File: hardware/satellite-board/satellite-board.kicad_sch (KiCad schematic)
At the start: 18 parts, among them J1 MTJ-88ARX1-FSM-LG, J2 B2B-PH-K-S, U1 LORA1262-915TCXO, U2 XC6220B331MR, U3 ESP32-C6-DEVKITC-1-N8, U4 MAX3485, U5 L70RE-M37

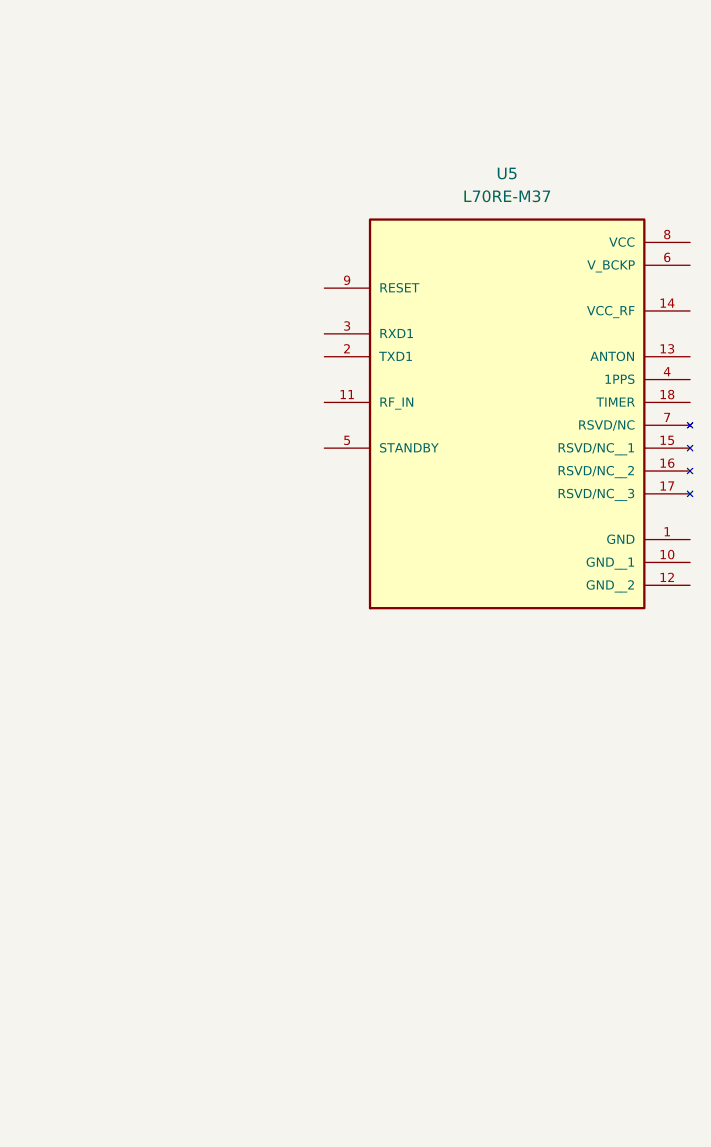
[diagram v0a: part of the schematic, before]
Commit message: New GPS module
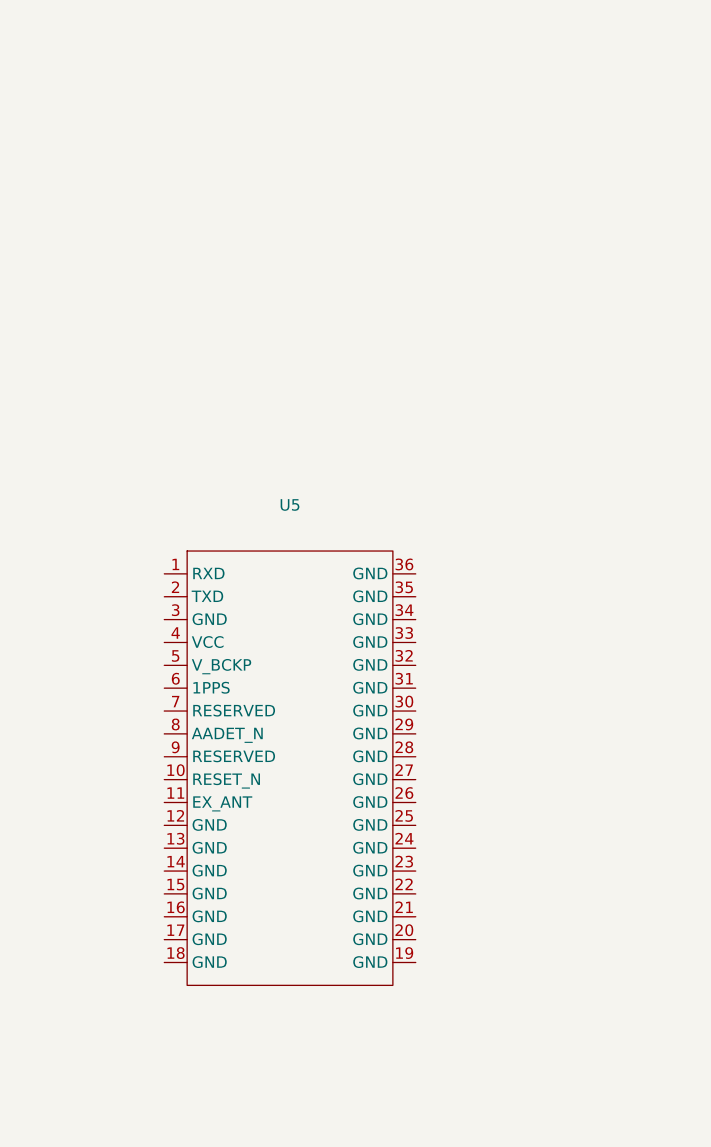
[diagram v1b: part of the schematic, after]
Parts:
- removed U5: L70RE-M37, footprints:XCVR_L70RE-M37, symbol L70RE-M37:L70RE-M37
- added U5: ~, 1234:GPSM-SMD_L18.4-W18.4-P2.54_LC86GLAMD, symbol 1234:LC86GLAMD
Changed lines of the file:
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@@
+	)
+	(symbol
+		(lib_id "1234:LC86GLAMD")
+		(at 327.66 107.95 0)
+		(unit 1)
+		(exclude_from_sim no)
+		(in_bom yes)
+		(on_board yes)
+		(dnp no)
+		(fields_autoplaced yes)
+		(property "Reference" "U5"
+			(at 326.39 77.47 0)
+			(effects
+				(font
+					(size 1.27 1.27)
+				)
+			)
+		)
+		(property "Value" "~"
+			(at 326.39 80.01 0)
+			(effects
+				(font
+					(size 1.27 1.27)
+				)
+			)
+		)
+		(property "Footprint" "1234:GPSM-SMD_L18.4-W18.4-P2.54_LC86GLAMD"
+			(at 327.66 107.95 0)
+			(effects
+				(font
+					(size 1.27 1.27)
+				)
+				(hide yes)
+			)
+		)
+		(property "Datasheet" "https://item.szlcsc.com/datasheet/LC86GLAMD/6880736.html"
+			(at 327.66 107.95 0)
+			(effects
+				(font
+					(size 1.27 1.27)
+				)
+				(hide yes)
+			)
+		)
+		(property "Description" ""
+			(at 327.66 107.95 0)
+			(effects
+				(font
+					(size 1.27 1.27)
+				)
+				(hide yes)
+			)
+		)
+		(property "Manufacturer Part" "LC86GLAMD"
+			(at 327.66 107.95 0)
+			(effects
+				(font
+					(size 1.27 1.27)
+				)
+				(hide yes)
+			)
+		)
+		(property "Manufacturer" "Quectel(移远)"
+			(at 327.66 107.95 0)
+			(effects
+				(font
+					(size 1.27 1.27)
+				)
+				(hide yes)
+			)
+		)
+		(property "Supplier Part" "C5943068"
+			(at 327.66 107.95 0)
+			(effects
+				(font
+					(size 1.27 1.27)
+				)
+				(hide yes)
+			)
+		)
+		(property "Supplier" "LCSC"
+			(at 327.66 107.95 0)
+			(effects
+				(font
+					(size 1.27 1.27)
+				)
+				(hide yes)
+			)
+		)
+		(property "LCSC Part Name" "LC86GLAMD"
+			(at 327.66 107.95 0)
+			(effects
+				(font
+					(size 1.27 1.27)
+				)
+				(hide yes)
+			)
+		)
+		(pin "25"
+		)
+		(pin "31"
+		)
+		(pin "24"
+		)
+		(pin "30"
+		)
+		(pin "26"
+		)
+		(pin "27"
+		)
+		(pin "28"
+		)
+		(pin "29"
+		)
+		(pin "23"
+		)
+		(pin "21"
+		)
+		(pin "22"
+		)
+		(pin "19"
+		)
+		(pin "20"
+		)
+		(pin "13"
+		)
+		(pin "14"
+		)
+		(pin "15"
+		)
+		(pin "16"
+		)
+		(pin "17"
+		)
+		(pin "36"
+		)
+		(pin "18"
+		)
+		(pin "35"
+		)
+		(pin "2"
+		)
+		(pin "9"
+		)
+		(pin "6"
+		)
+		(pin "10"
+		)
+		(pin "1"
+		)
+		(pin "12"
+		)
+		(pin "11"
+		)
+		(pin "3"
+		)
+		(pin "33"
+		)
+		(pin "5"
+		)
+		(pin "32"
+		)
+		(pin "34"
+		)
+		(pin "7"
+		)
+		(pin "8"
+		)
+		(pin "4"
+		)
+		(instances
+			(project ""
+				(path "/8ce565f0-183a-4bfb-874b-c5da5baf885e"
+					(reference "U5")
+					(unit 1)
+				)
+			)
+		)
 	)
 	(symbol
@@
 					(unit 1)
 				)
-			)
-		)
-	)
-	(symbol
-		(lib_id "L70RE-M37:L70RE-M37")
-		(at 350.52 60.96 0)
-		(unit 1)
-		(exclude_from_sim no)
-		(in_bom yes)
-		(on_board yes)
-		(dnp no)
-		(fields_autoplaced yes)
-		(property "Reference" "U5"
-			(at 350.52 40.64 0)
-			(effects
-				(font
-					(size 1.27 1.27)
-				)
-			)
-		)
-		(property "Value" "L70RE-M37"
-			(at 350.52 43.18 0)
-			(effects
-				(font
-					(size 1.27 1.27)
-				)
-			)
-		)
-		(property "Footprint" "footprints:XCVR_L70RE-M37"
-			(at 350.52 60.96 0)
-			(effects
-				(font
-					(size 1.27 1.27)
-				)
-				(justify bottom)
-				(hide yes)
-			)
-		)
-		(property "Datasheet" ""
-			(at 350.52 60.96 0)
-			(effects
-				(font
-					(size 1.27 1.27)
-				)
-				(hide yes)
-			)
-		)
-		(property "Description" ""
-			(at 350.52 60.96 0)
-			(effects
-				(font
-					(size 1.27 1.27)
-				)
-				(hide yes)
-			)
-		)
-		(property "MF" "Quectel"
-			(at 350.52 60.96 0)
-			(effects
-				(font
-					(size 1.27 1.27)
-				)
-				(justify bottom)
-				(hide yes)
-			)
-		)
-		(property "Description_1" "L70RE-M37, an SMD type module, brings the high performance of MTK positioning engine to the industrial applications with compact profile, ultra low power consumption and fast positioning capability."
-			(at 350.52 60.96 0)
-			(effects
-				(font
-					(size 1.27 1.27)
-				)
-				(justify bottom)
-				(hide yes)
-			)
-		)
-		(property "Package" "None"
-			(at 350.52 60.96 0)
-			(effects
-				(font
-					(size 1.27 1.27)
-				)
-				(justify bottom)
-				(hide yes)
-			)
-		)
-		(property "Price" "None"
-			(at 350.52 60.96 0)
-			(effects
-				(font
-					(size 1.27 1.27)
-				)
-				(justify bottom)
-				(hide yes)
-			)
-		)
-		(property "MP" "L70RE-M37"
-			(at 350.52 60.96 0)
-			(effects
-				(font
-					(size 1.27 1.27)
-				)
-				(justify bottom)
-				(hide yes)
-			)
-		)
-		(property "Availability" "In Stock"
-			(at 350.52 60.96 0)
-			(effects
-				(font
-					(size 1.27 1.27)
-				)
-				(justify bottom)
-				(hide yes)
-			)
-		)
-		(pin "13"
-		)
-		(pin "9"
-		)
-		(pin "2"
-		)
-		(pin "6"
-		)
-		(pin "4"
-		)
-		(pin "11"
-		)
-		(pin "5"
-		)
-		(pin "3"
-		)
-		(pin "8"
-		)
-		(pin "14"
-		)
-		(pin "16"
-		)
-		(pin "10"
-		)
-		(pin "17"
-		)
-		(pin "15"
-		)
-		(pin "12"
-		)
-		(pin "7"
-		)
-		(pin "1"
-		)
-		(pin "18"
-		)
-		(instances
-			(project ""
-				(path "/8ce565f0-183a-4bfb-874b-c5da5baf885e"
-					(reference "U5")
-					(unit 1)
-				)

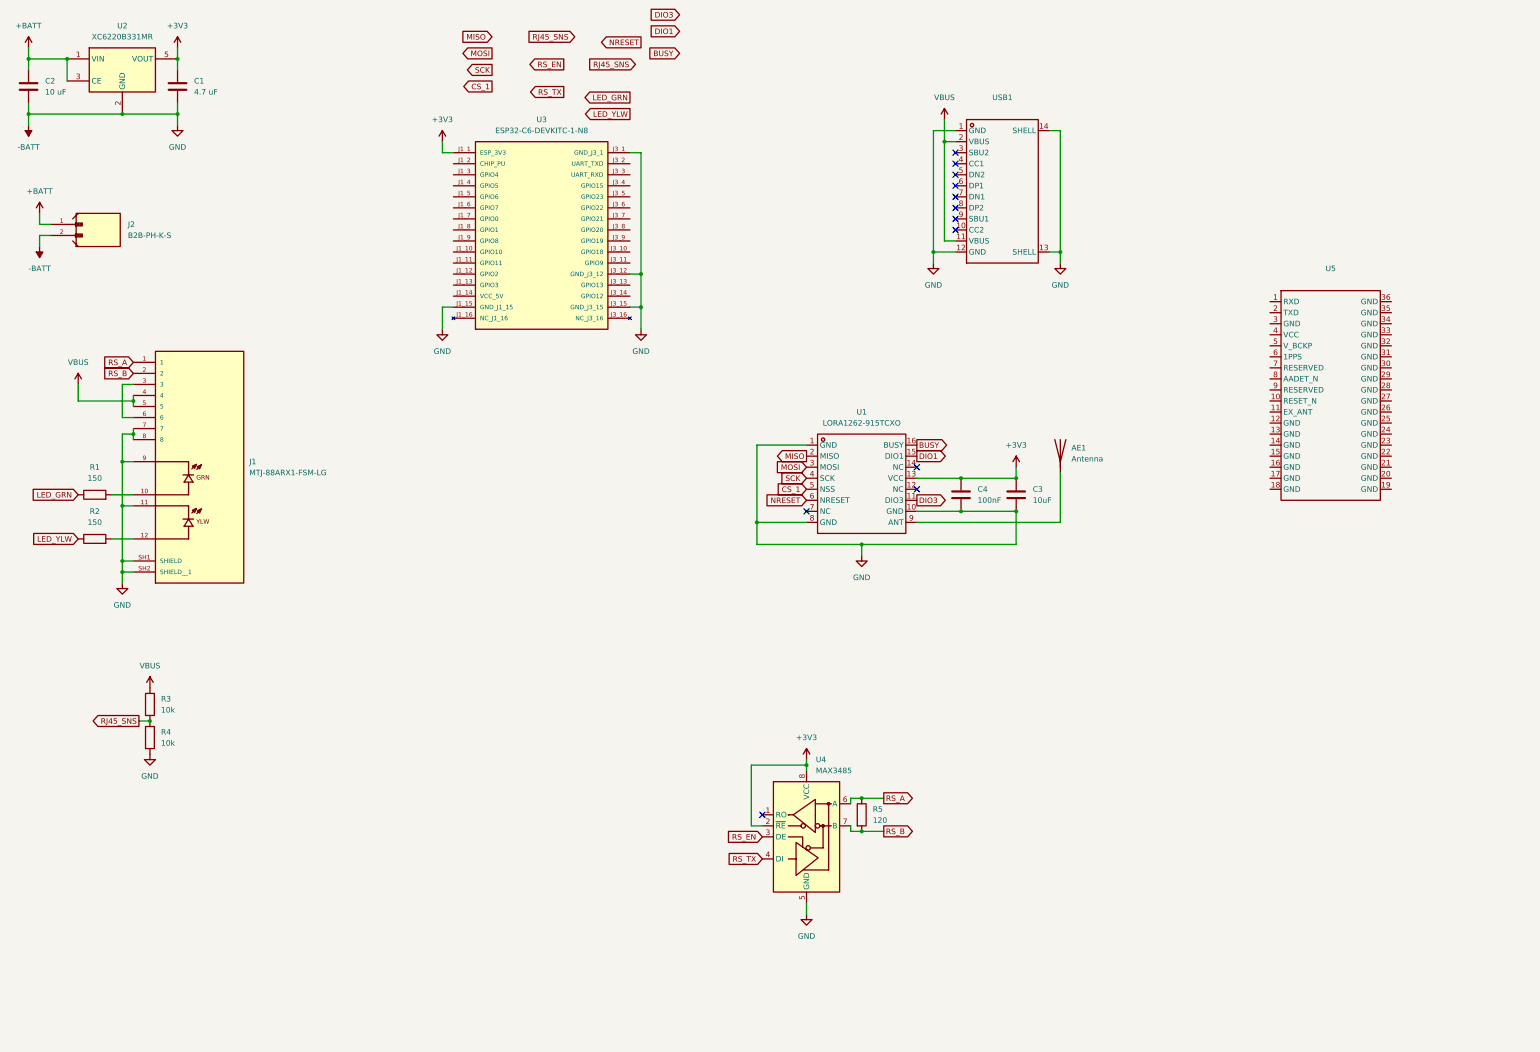
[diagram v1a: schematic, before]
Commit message: Everything added to satelite schematic,
Need to finish wiring MCU
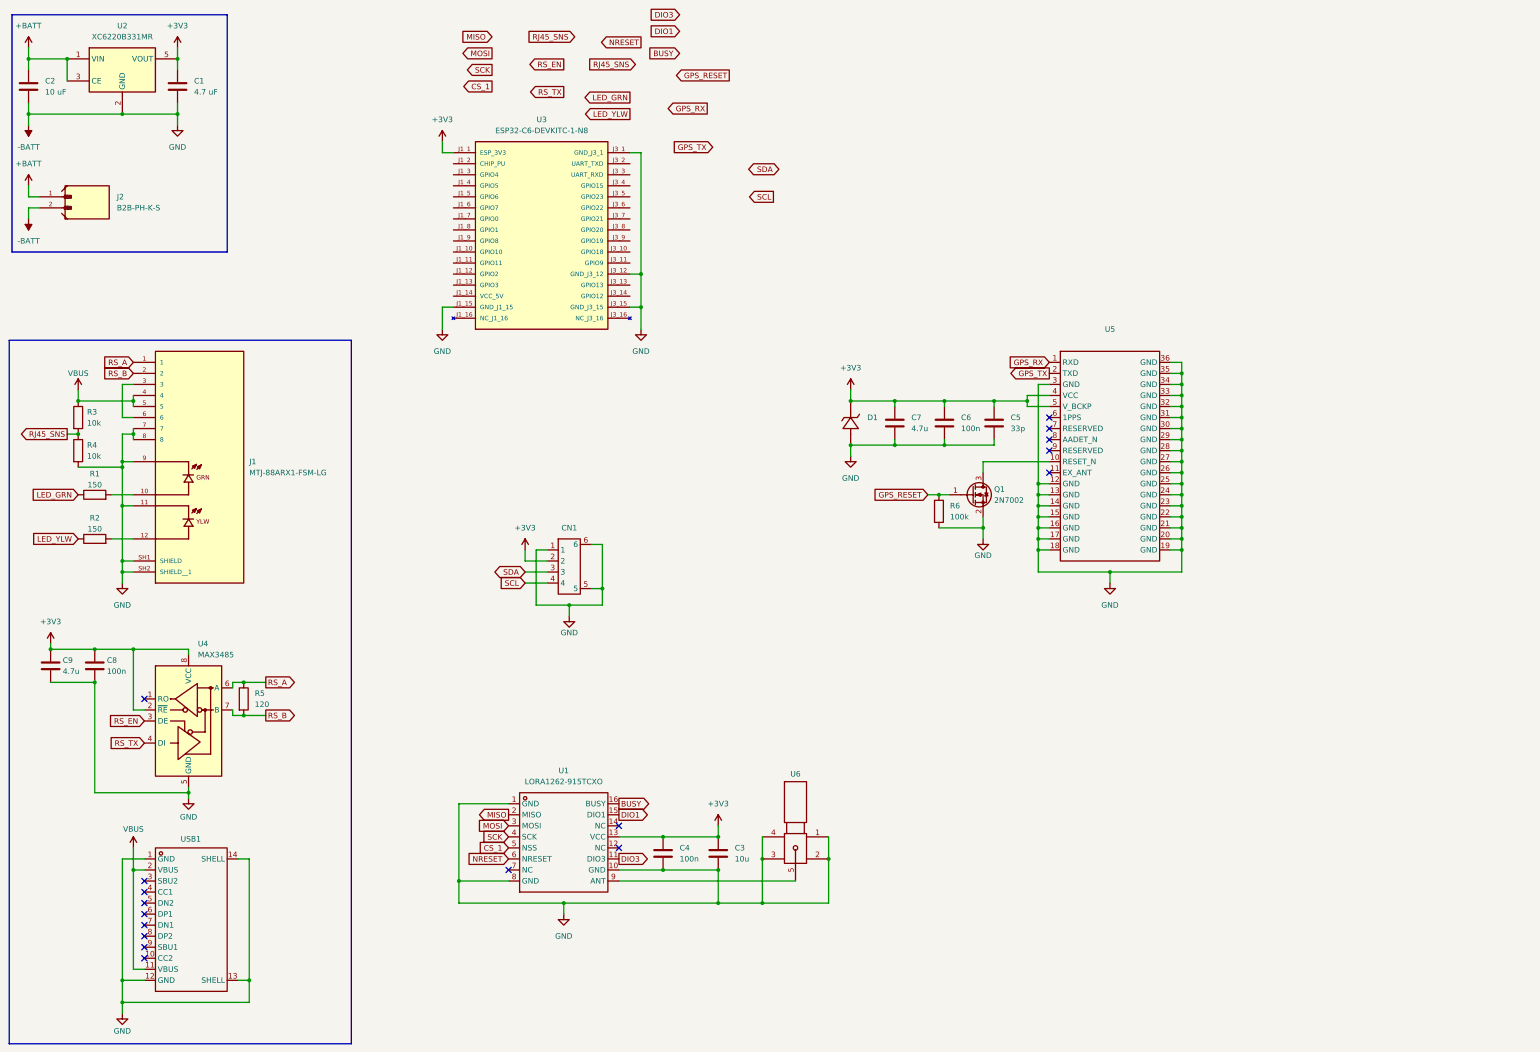
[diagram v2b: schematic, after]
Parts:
- removed AE1: Antenna, symbol Device:Antenna
- added C5: 33p, symbol Device:C
- added C6, C8: 100n, symbol Device:C
- added C7, C9: 4.7u, symbol Device:C
- added CN1: ~, library:CONN-SMD_4P-P1.00_XY-SM04B-SRSS-TB, symbol ProLib_pcs_2026-0sd2-01:XY-SM04B-SRSS-TB
- added D1: ~, Diode_SMD:D_SOD-323F, symbol 5678:PESD3V3L1UA_C7588061
- added Q1: 2N7002, Package_TO_SOT_SMD:SOT-23, symbol Transistor_FET:2N7002
- added R6: 100k, symbol Device:R
- added U6: ~, Library:SMA-TH_SMA-KWE_C7498154, symbol 123-02-01:SMA-KWE_C7498154
- C3: value 10uF -> 10u
- C4: value 100nF -> 100n
- U5: footprint 1234:GPSM-SMD_L18.4-W18.4-P2.54_LC86GLAMD -> library:GPSM-SMD_L18.4-W18.4-P2.54_LC86GLAMD
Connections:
- net +3V3: now also U5.4 (VCC), U5.5 (V_BCKP), C5.1, C6.1, C7.1, C8.1, C9.1, CN1.2, D1.1 (K)
- net -BATT: now also U5.12 (GND), U5.13 (GND), U5.14 (GND), U5.15 (GND), U5.16 (GND), U5.17 (GND), U5.18 (GND), U5.19 (GND), U5.20 (GND), U5.21 (GND), U5.22 (GND), U5.23 (GND), U5.24 (GND), U5.25 (GND), U5.26 (GND), U5.27 (GND), U5.28 (GND), U5.29 (GND), U5.3 (GND), U5.30 (GND), U5.31 (GND), U5.32 (GND), U5.33 (GND), U5.34 (GND), U5.35 (GND), U5.36 (GND), C5.2, C6.2, C7.2, C8.2, C9.2, CN1.1, CN1.5, CN1.6, D1.2 (A), Q1.2 (S), R6.2, U6.1, U6.2, U6.3, U6.4
- net GPS_RX: now reaches U5.1 (RXD)
- net at U5.10 (RESET_N): now also Q1.3 (D)
- net GPS_TX: now reaches U5.2 (TXD)
- net at U1.9 (ANT): now also U6.5
- new net GPS_RESET: Q1.1 (G), R6.1
- new net SCL: CN1.4
- new net SDA: CN1.3
- no-connect marks 12 -> 17
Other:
- moved on the sheet: C3, C4, J2, R3, R4, R5, U1, U4, U5, USB1

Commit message: Satelite Schematic Finished
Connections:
- net BUSY: now also U3.J3_5 (GPIO23)
- net CS_1: now also U3.J1_8 (GPIO1)
- net DIO1: now also U3.J3_6 (GPIO22)
- net GPS_RESET: now also U3.J3_8 (GPIO20)
- net GPS_RX: now also U3.J1_3 (GPIO4)
- net GPS_TX: now also U3.J1_4 (GPIO5)
- net LED_GRN: now also U3.J1_10 (GPIO10)
- net LED_YLW: now also U3.J1_11 (GPIO11)
- net MISO: now also U3.J1_12 (GPIO2)
- net MOSI: now also U3.J1_6 (GPIO7)
- net NRESET: now also U3.J1_7 (GPIO0)
- net RJ45_SNS: now also U3.J3_7 (GPIO21)
- net RS_EN: now also U3.J1_13 (GPIO3)
- net RS_TX: now also U3.J3_2 (UART_TXD)
- net SCK: now also U3.J1_5 (GPIO6)
- net SCL: now also U3.J3_9 (GPIO19)
- net SDA: now also U3.J3_10 (GPIO18)
- net DIO3: no longer names the net of U1.11 (DIO3)
- no-connect marks 17 -> 26
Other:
- note added: "ESP32-C6 MCU"
- note added: "GPS MODULE"
- note added: "I/O COMPONENTS"
- note added: "I2C BUS"
- note added: "LORA MODULE"
- note added: "PWR SYSTEM"
- moved on the sheet: C1, C2, C3, C4, C5, C6, C7, C8, C9, CN1, D1, J1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

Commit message: updates to central
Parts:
- R3: value 10k -> 14k
- R4: value 10k -> 6k
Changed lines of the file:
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@@
 			)
 		)
-		(property "Value" "10k"
+		(property "Value" "6k"
 			(at 178.562 85.09 0)
 			(effects
@@
 			)
 		)
-		(property "Value" "10k"
+		(property "Value" "14k"
 			(at 178.562 77.47 0)
 			(effects

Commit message: Satelite & Central Schematic Finished
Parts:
- R3: value 14k -> 15K
- R4: value 6k -> 5K
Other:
- moved on the sheet: C1, C2, C3, C4, C5, C6, C7, C8, C9, CN1, D1, J1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

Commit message: LCSC for Sat.
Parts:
- C1: value 4.7 uF -> 4.7u; footprint (none) -> Capacitor_SMD:C_0805_2012Metric; LCSC (none) -> C1779
- C2: value 10 uF -> 10u; footprint (none) -> Capacitor_SMD:C_0603_1608Metric; LCSC (none) -> C19702
- C3: footprint (none) -> Capacitor_SMD:C_0603_1608Metric; LCSC (none) -> C19702
- C4, C6, C8: footprint (none) -> Capacitor_SMD:C_0402_1005Metric; LCSC (none) -> C1525
- C5: footprint (none) -> Capacitor_SMD:C_0402_1005Metric; LCSC (none) -> C1562
- C7, C9: footprint (none) -> Capacitor_SMD:C_0805_2012Metric; LCSC (none) -> C1779
- D1: LCSC (none) -> C7588061
- J1: footprint MTJ-88ARX1-FSM-LG:ADAMTECH_MTJ-88ARX1-FSM-LG -> footprints:ADAMTECH_MTJ-88ARX1-FSM-LG
- J2: footprint B2B-PH-K-S:JST_B2B-PH-K-S -> Connector_JST:JST_PH_B2B-PH-K_1x02_P2.00mm_Vertical
- Q1: LCSC (none) -> C8545
- R1, R2: footprint (none) -> Resistor_SMD:R_0603_1608Metric; LCSC (none) -> C22808
- R3: footprint (none) -> Resistor_SMD:R_0603_1608Metric; LCSC (none) -> C22809
- R4: value 5K -> 4.7k; footprint (none) -> Resistor_SMD:R_1206_3216Metric; LCSC (none) -> C17936
- R5: footprint (none) -> Resistor_SMD:R_0805_2012Metric; LCSC (none) -> C17437
- R6: footprint (none) -> Resistor_SMD:R_0402_1005Metric; LCSC (none) -> C25741
- U1: LCSC (none) -> C5356643
- U2: LCSC (none) -> C86534
- U3: footprint ESP32-C6-DEVKITC-1-N8:MODULE_ESP32-C6-DEVKITC-1-N8 -> footprints:MODULE_ESP32-C6-DEVKITC-1-N8
- U4: LCSC (none) -> C668204
- U5: LCSC (none) -> C5943068
- U6: LCSC (none) -> C7498154
- USB1: LCSC (none) -> C2765186
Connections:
- net -BATT renamed GND

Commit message: Satelite Board Started
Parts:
- removed D1: ~, Diode_SMD:D_SOD-323F, symbol 5678:PESD3V3L1UA_C7588061
- removed Q1: 2N7002, Package_TO_SOT_SMD:SOT-23, symbol Transistor_FET:2N7002
- added Q1: MMBT3904, Package_TO_SOT_SMD:SOT-23, symbol Transistor_BJT:MMBT3904
- added R7: 4.7k, Resistor_SMD:R_0402_1005Metric, symbol Device:R
- R6: value 100k -> 47k; LCSC C25741 -> C25792
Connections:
- net BUSY: now also U3.J1_13 (GPIO3); no longer U3.J3_5 (GPIO23)
- net GND: now also Q1.2 (E)
- net GPS_RESET: now also R7.1; no longer R6.1
- net RS_EN: now also U3.J3_5 (GPIO23); no longer U3.J1_13 (GPIO3)
- net at U5.10 (RESET_N): now also Q1.3 (C)
- new net: Q1.1 (B), R6.1, R7.2
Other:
- moved on the sheet: R6

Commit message: Updates to Sat
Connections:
- net DIO1: now also U3.J1_11 (GPIO11); no longer U3.J3_6 (GPIO22)
- net LED_GRN: now also U3.J3_7 (GPIO21); no longer U3.J1_10 (GPIO10)
- net LED_YLW: now also U3.J3_6 (GPIO22); no longer U3.J1_11 (GPIO11)
- net RJ45_SNS: now also U3.J1_10 (GPIO10); no longer U3.J3_7 (GPIO21)
